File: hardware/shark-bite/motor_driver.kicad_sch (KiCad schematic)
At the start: 42 parts, among them U10 IRFH7440TRPBF, U11 IRFH7440TRPBF, U12 IRFH7440TRPBF, U4 GD32E230G6U6TR, U5 FD6288Q, U6 AOZ1282CI, U7 IRFH7440TRPBF, U8 IRFH7440TRPBF, U9 IRFH7440TRPBF

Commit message: Routed Without Debug
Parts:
- added J6: Conn_01x03_Pin, Sharkbite:ESC Pads, symbol Connector:Conn_01x03_Pin
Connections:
- net OUT_A: now also J6.3 (Pin_3)
- net OUT_B: now also J6.2 (Pin_2)
- net OUT_C: now also J6.1 (Pin_1)
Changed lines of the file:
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@@
+    )
+  )
+  (global_label "OUT_B" (shape input) (at 257.81 98.425 180) (fields_autoplaced)
+    (effects (font (size 1.27 1.27)) (justify right))
+    (property "Intersheetrefs" "${INTERSHEET_REFS}" (at 248.8635 98.425 0)
+      (effects (font (size 1.27 1.27)) (justify right) hide)
     )
   )
@@
     )
   )
+  (global_label "OUT_A" (shape input) (at 257.81 95.885 180) (fields_autoplaced)
+    (effects (font (size 1.27 1.27)) (justify right))
+    (property "Intersheetrefs" "${INTERSHEET_REFS}" (at 249.0449 95.885 0)
+      (effects (font (size 1.27 1.27)) (justify right) hide)
+    )
+  )
   (global_label "OUT_B" (shape input) (at 93.345 152.4 0) (fields_autoplaced)
     (effects (font (size 1.27 1.27)) (justify left))
@@
     (property "Intersheetrefs" "${INTERSHEET_REFS}" (at 78.1011 65.405 0)
       (effects (font (size 1.27 1.27)) (justify left) hide)
+    )
+  )
+  (global_label "OUT_C" (shape input) (at 257.81 100.965 180) (fields_autoplaced)
+    (effects (font (size 1.27 1.27)) (justify right))
+    (property "Intersheetrefs" "${INTERSHEET_REFS}" (at 248.8635 100.965 0)
+      (effects (font (size 1.27 1.27)) (justify right) hide)
     )
   )
@@
         )
       )
+    )
+  )
+  (symbol (lib_id "Connector:Conn_01x03_Pin") (at 262.89 98.425 180) (unit 1)
+    (in_bom yes) (on_board yes) (dnp no) (fields_autoplaced)
+    (property "Reference" "J6" (at 263.6012 97.2129 0)
+      (effects (font (size 1.27 1.27)) (justify right))
+    )
+    (property "Value" "Conn_01x03_Pin" (at 263.6012 99.6371 0)
+      (effects (font (size 1.27 1.27)) (justify right))
+    )
+    (property "Footprint" "Sharkbite:ESC Pads" (at 262.89 98.425 0)
+      (effects (font (size 1.27 1.27)) hide)
+    )
+    (property "Datasheet" "~" (at 262.89 98.425 0)
+      (effects (font (size 1.27 1.27)) hide)
+    )
+    (pin "1")
+    (pin "2")
+    (pin "3")
+    (instances
+      (project "malenki-hv"
+        (path "/f41619e3-8cf2-4511-8a51-762d4de43197/b339fba4-a8e4-4c66-ad9c-610bd968ae93"
+          (reference "J6") (unit 1)
+        )
+      )

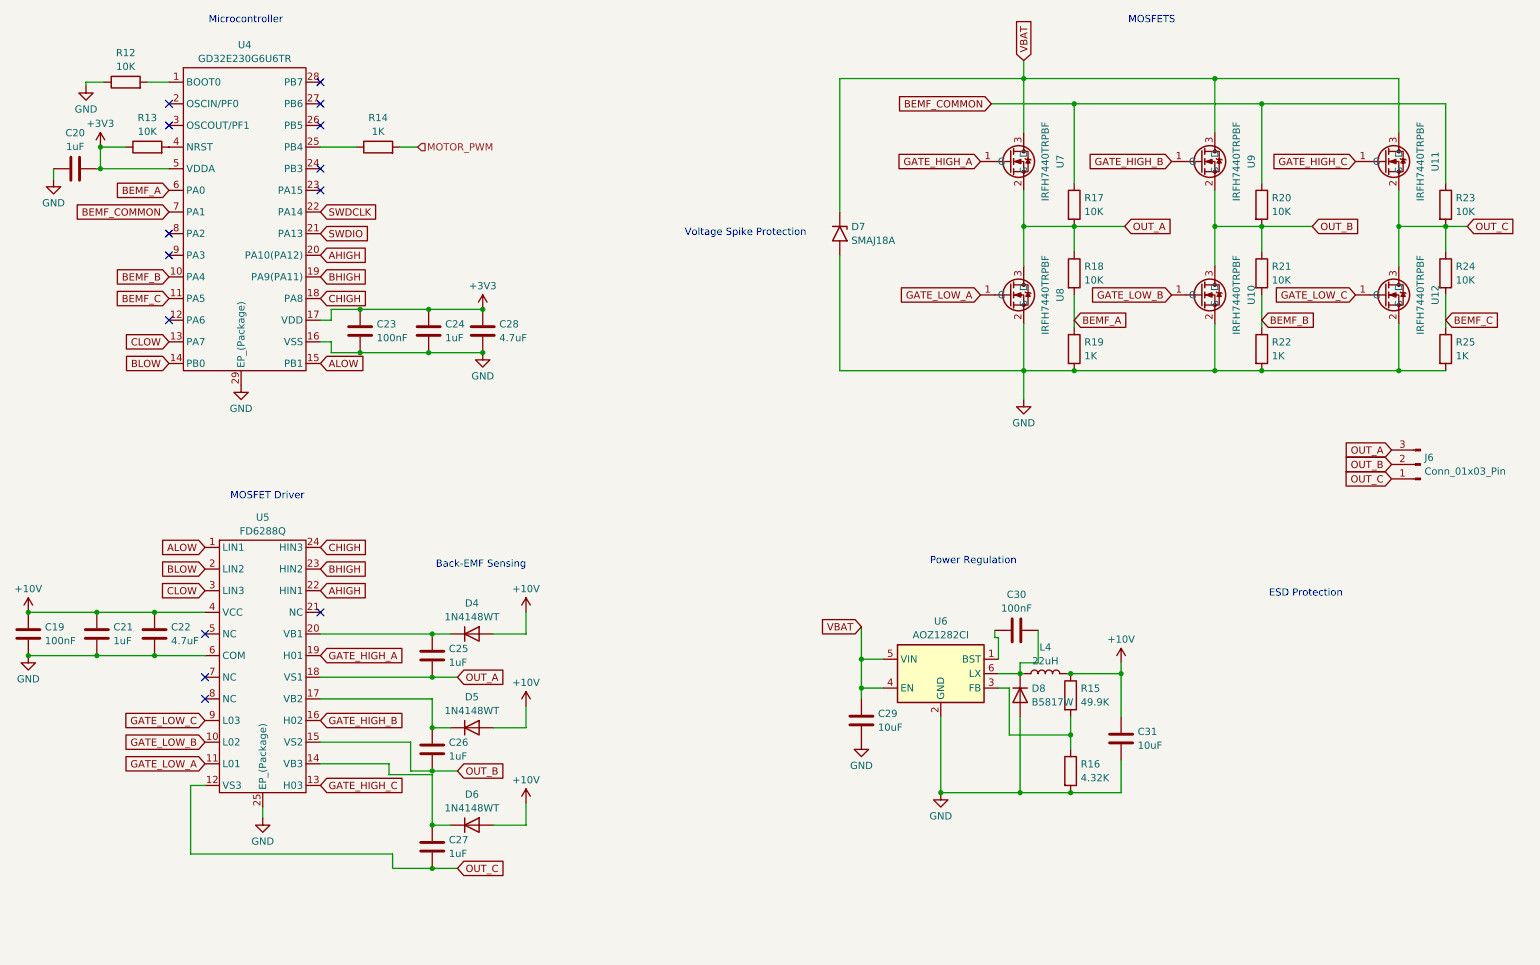
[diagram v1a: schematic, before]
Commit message: Added Gate Resistors and Power Capacitors
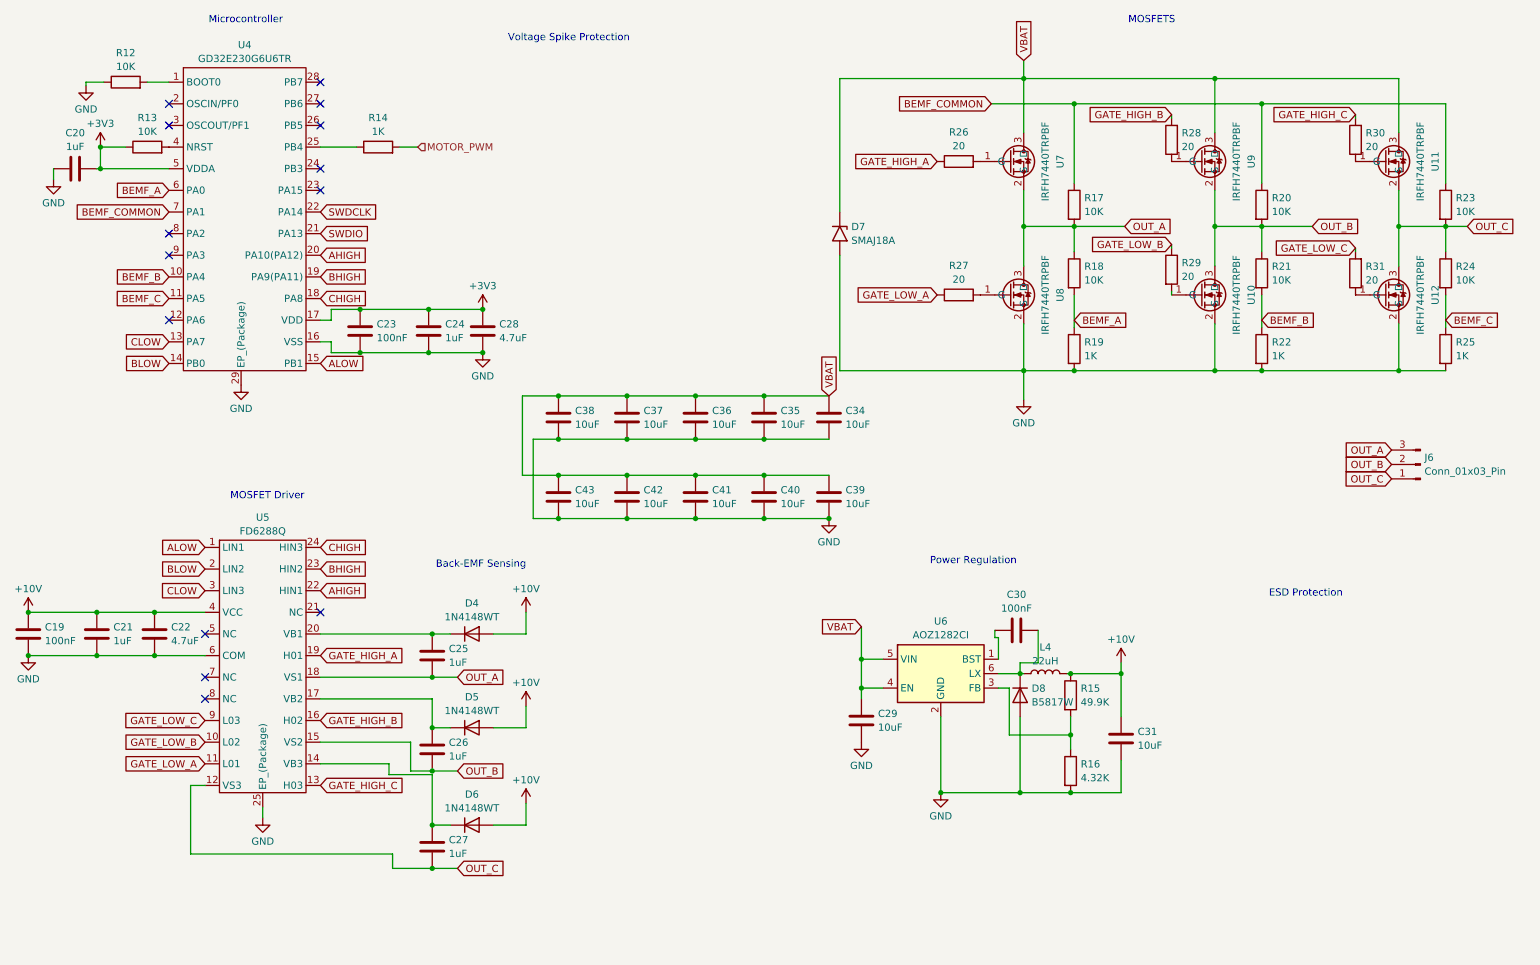
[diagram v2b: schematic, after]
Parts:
- added C34, C35, C36, C37, C38, C39, C40, C41, C42, C43: 10uF, Capacitor_SMD:C_0603_1608Metric, symbol Device:C
- added R26, R27, R28, R29, R30, R31: 20, Resistor_SMD:R_0402_1005Metric, symbol Device:R
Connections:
- net GATE_HIGH_A: now also R26.1; no longer U7.1 (G)
- net GATE_HIGH_B: now also R28.2; no longer U9.1 (G)
- net GATE_HIGH_C: now also R30.2; no longer U11.1 (G)
- net GATE_LOW_A: now also R27.1; no longer U8.1 (G)
- net GATE_LOW_B: now also R29.1; no longer U10.1 (G)
- net GATE_LOW_C: now also R31.2; no longer U12.1 (G)
- net GND: now also C34.2, C35.2, C36.2, C37.2, C38.2, C39.2, C40.2, C41.2, C42.2, C43.2
- net VBAT: now also C34.1, C35.1, C36.1, C37.1, C38.1, C39.1, C40.1, C41.1, C42.1, C43.1
- new net: R31.1, U12.1 (G)
- new net: R27.2, U8.1 (G)
- new net: R28.1, U9.1 (G)
- new net: R26.2, U7.1 (G)
- new net: R30.1, U11.1 (G)
- new net: R29.2, U10.1 (G)

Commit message: V0
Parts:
- removed C25, C26, C27: 1uF, Capacitor_SMD:C_0402_1005Metric_Pad0.74x0.62mm_HandSolder, symbol Device:C
- removed C29, C31: 10uF, Capacitor_SMD:C_0402_1005Metric_Pad0.74x0.62mm_HandSolder, symbol Device:C
- removed C30: 100nF, Capacitor_SMD:C_0402_1005Metric_Pad0.74x0.62mm_HandSolder, symbol Device:C
- removed D4, D5, D6: 1N4148WT, Diode_SMD:D_SOD-523, symbol Diode:1N4148WT
- removed D8: B5817W, Diode_SMD:D_SOD-123, symbol Device:D
- removed L4: 22uH, Inductor_SMD:L_Bourns_SRP7028A_7.3x6.6mm, symbol Device:L
- removed R15: 49.9K, Resistor_SMD:R_0402_1005Metric, symbol Device:R
- removed R16: 4.32K, Resistor_SMD:R_0402_1005Metric, symbol Device:R
- removed U5: FD6288Q, Package_DFN_QFN:QFN-24-1EP_4x4mm_P0.5mm_EP2.65x2.65mm, symbol Sharkbite:FD6288Q
- removed U6: AOZ1282CI, Package_TO_SOT_SMD:SOT-23-6, symbol Regulator_Switching:AOZ1282CI
- added C3, C4, C5: 100nF, Capacitor_SMD:C_0402_1005Metric_Pad0.74x0.62mm_HandSolder, symbol Device:C
- added C7, C8, C9: 100nF, Capacitor_SMD:C_0603_1608Metric, symbol Device:C
- added J3: PWM Pads, symbol Connector:Conn_01x02_Pin
- added TP1, TP2: TestPoint, symbol Connector:TestPoint
- added U2: DRV8300DRGER, RGE0024B-IPC_A, symbol Sharkbite:DRV8300DRGER
- C22: value 4.7uF -> 10uF (X5R)
- J6: value Conn_01x03_Pin -> Motor Pads
- R26, R27, R28, R29, R30, R31: value 20 -> 2.2
- U10, U11, U12, U7, U8, U9: value IRFH7440TRPBF -> SISS54; footprint Sharkbite:PQFN FET -> Package_DFN_QFN:Infineon_PQFN-22-15-4EP_6x5mm_P0.65mm
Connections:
- net +10V: now also U2.4 (GVDD)
- net AHIGH: now also U2.22 (INHA)
- net ALOW: now also U2.1 (INLA)
- net BHIGH: now also U2.23 (INHB)
- net BLOW: now also U2.2 (INLB)
- net CHIGH: now also U2.24 (INHC)
- net CLOW: now also U2.3 (INLC)
- net GND: now also C7.2, C8.2, C9.2, J3.1 (Pin_1), U2.25 (PowerPAD), U2.6 (GND)
- net SWDCLK: now also TP1.1
- net SWDIO: now also TP2.1
- net BEMF_COMMON renamed BEMF_COM
- net GATE_HIGH_A renamed GHA
- net GHA: now also U2.19 (GHA)
- net GATE_HIGH_B renamed GHB
- net GHB: now also U2.16 (GHB)
- net GATE_HIGH_C renamed GHC
- net GHC: now also U2.13 (GHC)
- net GATE_LOW_A renamed GLA
- net GLA: now also U2.11 (GLA)
- net GATE_LOW_B renamed GLB
- net GLB: now also U2.10 (GLB)
- net GATE_LOW_C renamed GLC
- net GLC: now also U2.9 (GLC)
- net MOTOR_PWM renamed PWM
- net PWM: now also J3.2 (Pin_2)
- net VBAT renamed VBUS
- net VBUS: now also C7.1, C8.1, C9.1
- new net: C5.2, U2.12 (SHC)
- new net: C5.1, U2.14 (BSTC)
- new net: C4.2, U2.15 (SHB)
- new net: C4.1, U2.17 (BSTB)
- new net: C3.2, U2.18 (SHA)
- new net: C3.1, U2.20 (BSTA)
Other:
- note removed: "Back-EMF Sensing"
- note removed: "ESD Protection"
- note removed: "Power Regulation"
- note removed: "Voltage Spike Protection"
- moved on the sheet: C19, C21, C22, C23, C24, C28, C34, C35, C36, C37, C38, C39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

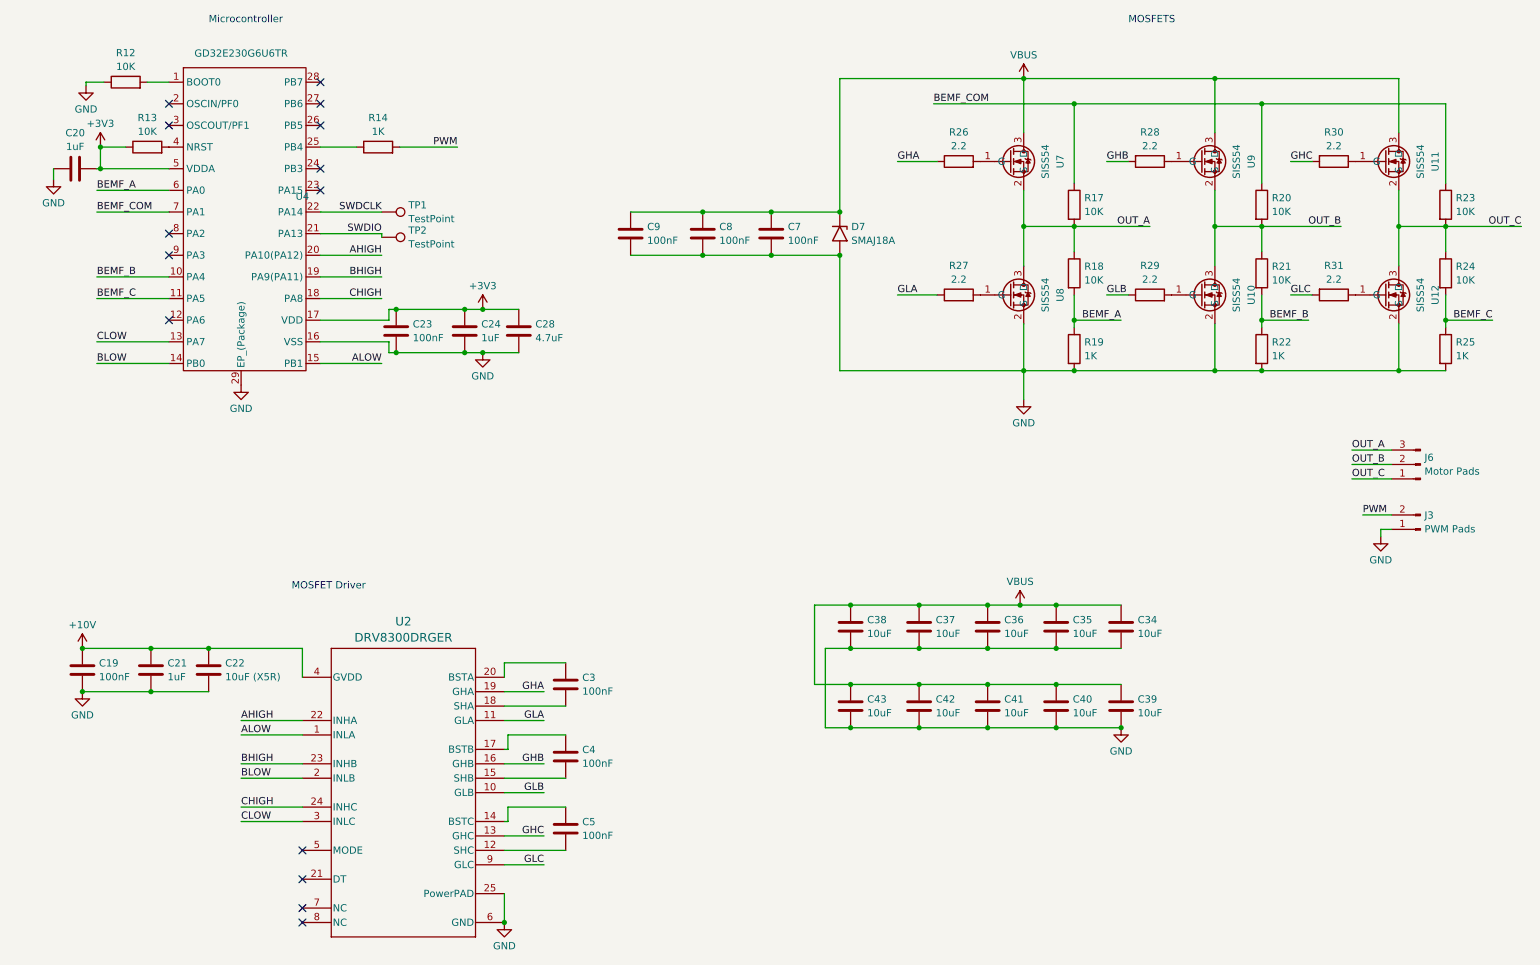
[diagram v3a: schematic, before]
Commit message: Added tag-connect
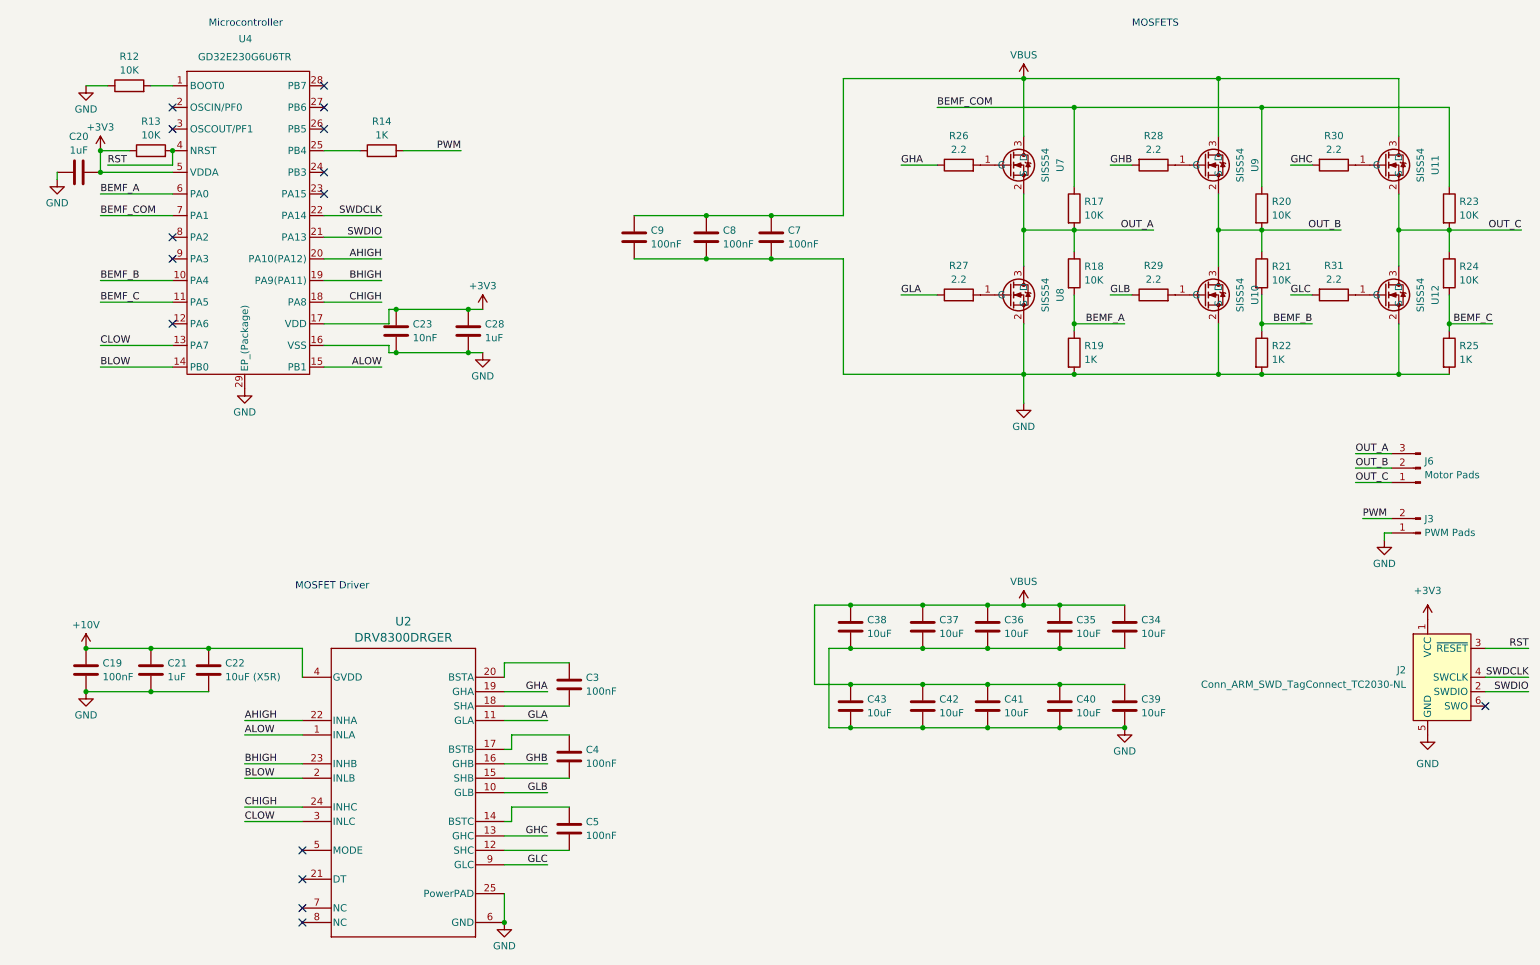
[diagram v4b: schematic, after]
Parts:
- removed C24: 1uF, Capacitor_SMD:C_0402_1005Metric_Pad0.74x0.62mm_HandSolder, symbol Device:C
- removed D7: SMAJ18A, Diode_SMD:D_SMA, symbol Diode:SMAJ18A
- removed TP1, TP2: TestPoint, symbol Connector:TestPoint
- added J2: Conn_ARM_SWD_TagConnect_TC2030-NL, Connector:Tag-Connect_TC2030-IDC-NL_2x03_P1.27mm_Vertical, symbol Connector:Conn_ARM_SWD_TagConnect_TC2030-NL
- C23: value 100nF -> 10nF
- C28: value 4.7uF -> 1uF
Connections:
- net +3V3: now also J2.1 (VCC)
- net GND: now also J2.5 (GND)
- net SWDCLK: now also J2.4 (SWCLK)
- net SWDIO: now also J2.2 (SWDIO)
- net RST: now reaches R13.2, U4.4 (NRST)
- net RST: now also J2.3 (~{RESET})
- no-connect marks 14 -> 15
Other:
- moved on the sheet: C19, C20, C28, C3, C34, C35, C37, C39, C4, C40, C42, C5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
